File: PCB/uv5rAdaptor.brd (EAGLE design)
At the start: 13.9 x 13.9 mm, 2 parts

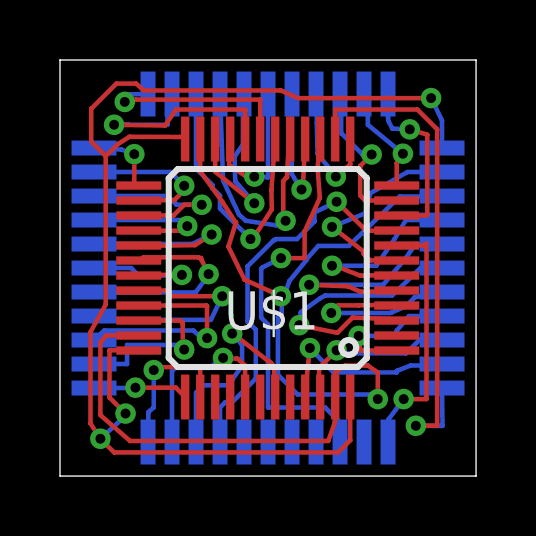
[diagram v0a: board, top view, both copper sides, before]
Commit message: Changed OSC pins to OSC32
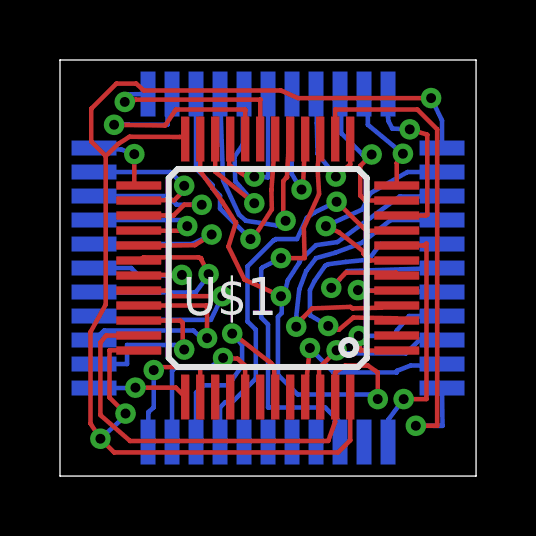
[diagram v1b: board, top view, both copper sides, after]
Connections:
- net GPIO6: now also U$1.6; no longer U$1.3
- net OSC_IN: now also U$1.3; no longer U$1.5
- net OSC_OUT: now also U$1.4; no longer U$1.6
- net VOX: now also U$1.5; no longer U$1.4
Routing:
- net OSC_OUT: track 6.74 -> 10.7 mm
- net GPIO6: track 9.18 -> 6.43 mm
- net VOX: track 6.19 -> 4.14 mm
- net OSC_IN: track 8.06 -> 9.20 mm
